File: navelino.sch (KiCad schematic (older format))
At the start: 73 parts, among them CON1 USB, IC1 ATMEGA328P-A, M1 CONN_1, M2 CONN_1, P1 CONN_02X03, P3 CONN_6, SW0 SW_PUSH, SW1 SMD-SWITCH-TACTILE-SPST-NO(4P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, SW2 SMD-SWITCH-TACTILE-SPST-NO(4P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, U1 XC6204B332MR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

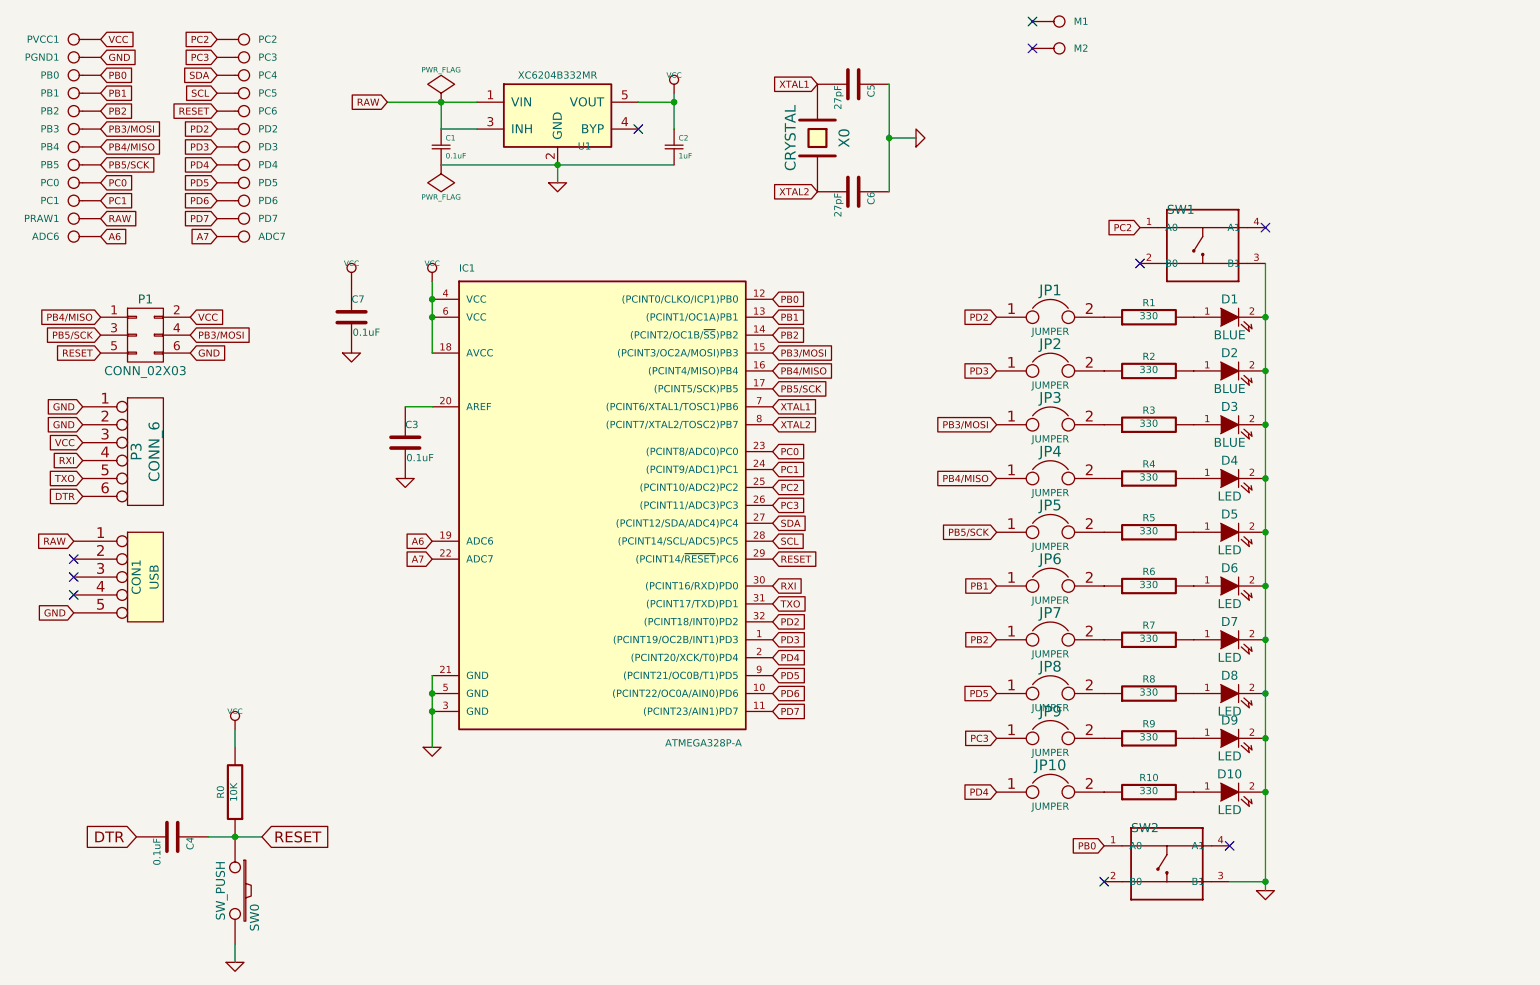
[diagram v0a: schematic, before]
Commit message: Empezando rev3
- Permitir hojas intercambiables, conector SPI completo
- Usar charlieplexing para reducir el numero de GPIOS para los leds a 4
en vez de 10
- Eliminar el botón de reset, se usara una pulsación prolongada de los
dos botones de disparo para hacer un reset software
- Añadir soporte V-USB en el cuerpo
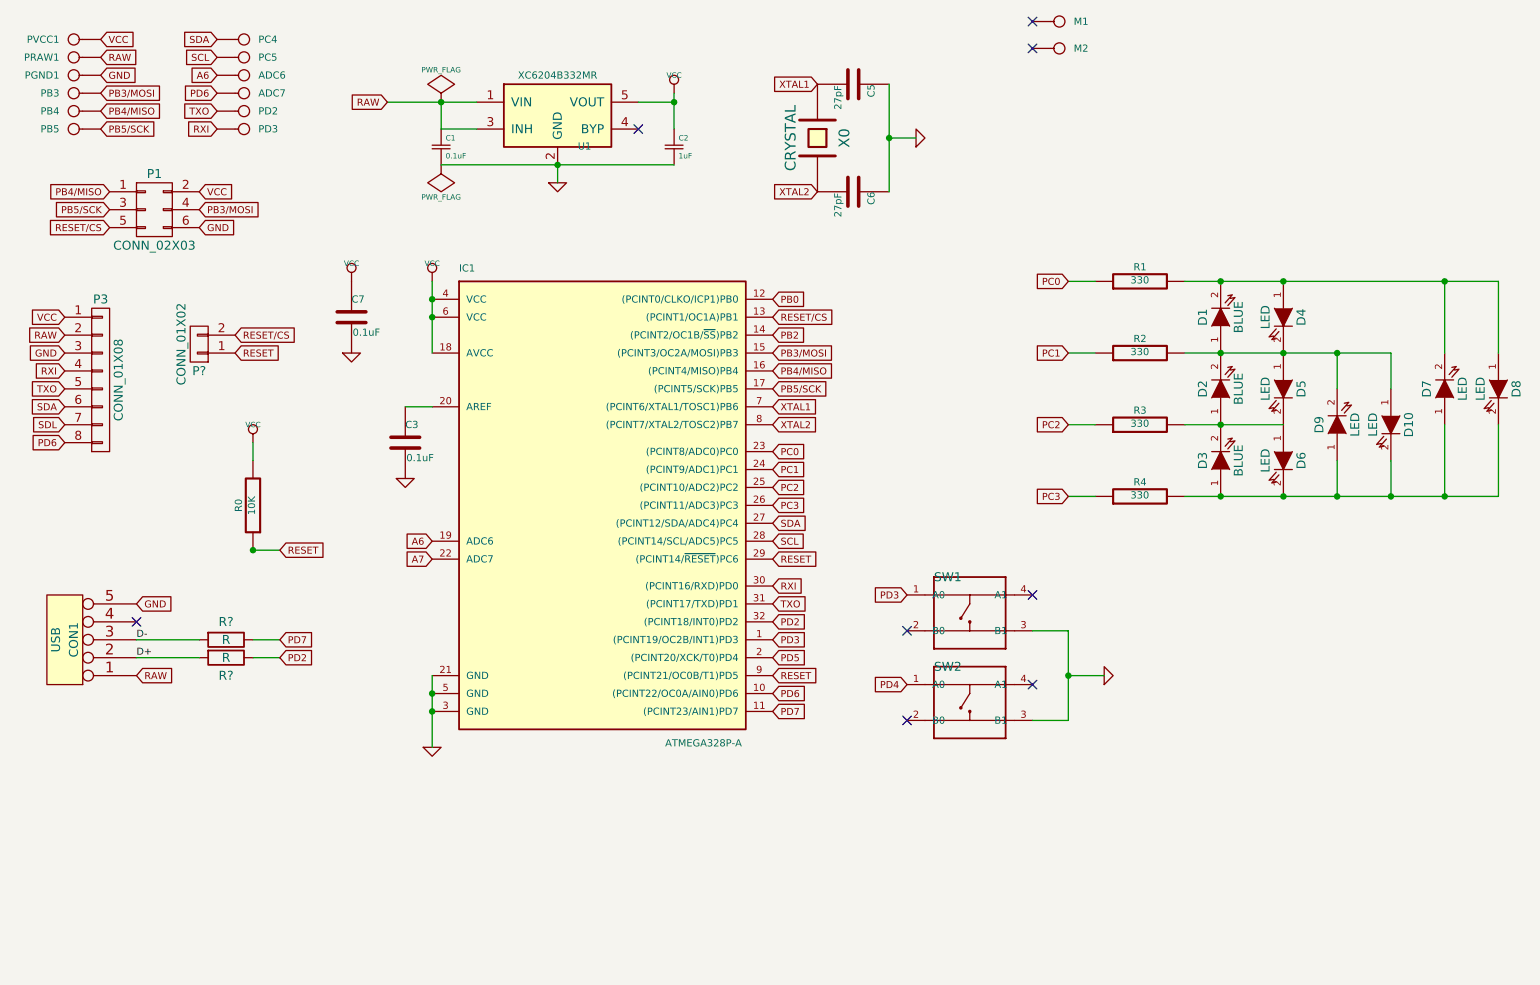
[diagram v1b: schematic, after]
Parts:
- removed C4: 0.1uF, navelino:C_0805, symbol C-RESCUE-navelino
- removed JP1, JP10, JP2, JP3, JP4, JP5, JP6, JP7, JP8, JP9: JUMPER, navelino:PCB_JUMPER, symbol JUMPER
- removed P3: CONN_6, navelino:Pin_Header_Angled_1x06, symbol CONN_6
- removed PB0, PB1, PB2, PC0, PC1, PC2, PC3, PC6, PD4, PD5, PD6, PD7: CONN_1, navelino:SolderWirePad_single_1mmDrill, symbol CONN_1
- removed R10, R5, R6, R7, R8, R9: 330, navelino:R_0805_HandSoldering, symbol R-RESCUE-navelino
- removed SW0: SW_PUSH, navelino:B3U-1000P, symbol SW_PUSH
- added P3: CONN_01X08, symbol CONN_01X08
- added P?: CONN_01X02, symbol CONN_01X02
- added R? (x2): R, symbol R
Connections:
- net A7: no longer ADC7.1
- net GND: now also P3.3 (P3); no longer D1.2 (K), D10.2 (K), D2.2 (K), D3.2 (K), D4.2 (K), D5.2 (K), D6.2 (K), D7.2 (K), D8.2 (K), D9.2 (K)
- net PB0: no longer SW2.1 (A0)
- net PC0: now also R1.1
- net PC1: now also R2.1
- net PC2: now also R3.1; no longer SW1.1 (A0)
- net PC3: now also R4.1
- net PD2: now also R?.1; no longer PD2.1
- net PD3: now also SW1.1 (A0); no longer PD3.1
- net PD4: now also SW2.1 (A0); no longer IC1.2 ((PCINT20/XCK/T0)PD4)
- net PD5: now also IC1.2 ((PCINT20/XCK/T0)PD4); no longer IC1.9 ((PCINT21/OC0B/T1)PD5)
- net PD6: now also ADC7.1, P3.8 (P8)
- net PD7: now also R?.1
- net RAW: now also P3.2 (P2)
- net RESET: now also IC1.9 ((PCINT21/OC0B/T1)PD5), P?.1 (P1); no longer P1.5 (P5)
- net RXI: now also PD3.1, P3.4 (P4)
- net SDA: now also P3.6 (P6)
- net TXO: now also PD2.1, P3.5 (P5)
- net VCC: now also P3.1 (P1)
- net at D1.1 (A): now also D10.1 (A), D2.2 (K), D4.2 (K), D5.1 (A), D9.2 (K), R2.2; no longer R1.2
- net at D2.1 (A): now also D3.2 (K), D5.2 (K), D6.1 (A), R3.2; no longer R2.2
- net at D3.1 (A): now also D10.2 (K), D6.2 (K), D7.1 (A), D8.2 (K), D9.1 (A), R4.2; no longer R3.2
- net at D4.1 (A): now also D1.2 (K), D7.2 (K), D8.1 (A), R1.2; no longer R4.2
- net D+: now reaches CON1.2
- net D+: now also R?.2
- net D-: now reaches CON1.3
- net D-: now also R?.2
- net PB1 renamed RESET/CS
- net RESET/CS: now also P1.5 (P5), P?.2 (P2)
- new net SDL: P3.7 (P7)
- no-connect marks 10 -> 8
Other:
- moved on the sheet: ADC6, ADC7, CON1, D1, D10, D2, D3, D4, D5, D6, D7, D8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

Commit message: Casi finalizado el nuevo esquema
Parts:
- removed M1, M2: CONN_1, navelino:SolderWirePad_single_1mmDrill, symbol CONN_1
- removed P1: CONN_02X03, navelino:ISPSMD, symbol CONN_02X03
- removed P?: CONN_01X02, symbol CONN_01X02
- added P1: CONN_02X04, symbol CONN_02X04
- added R5: R, symbol R
- R6, R7: renamed from R?; value R -> 68
- renumbered PB3 to PB0, PB4 to PB1, PB5 to PB2
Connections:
- net PB0 is gone; now on net RESET: IC1.12 ((PCINT0/CLKO/ICP1)PB0)
- net SDL is gone; now on net SCL: P3.7 (P7)
- net A6: now also PD3.1; no longer ADC6.1
- net A7: now also PB2.1
- net D-: now also R5.2
- net GND: now also P1.6 (P6)
- net PB3/MOSI: now also P1.4 (P4); no longer PB0.1
- net PB4/MISO: now also P1.1 (P1); no longer PB1.1
- net PB5/SCK: now also P1.3 (P3); no longer PB2.1
- net PD4: now also IC1.2 ((PCINT20/XCK/T0)PD4)
- net PD5: now also IC1.9 ((PCINT21/OC0B/T1)PD5), PB1.1; no longer IC1.2 ((PCINT20/XCK/T0)PD4)
- net PD6: now also PD2.1; no longer ADC7.1
- net RESET: now also P1.5 (P5); no longer IC1.9 ((PCINT21/OC0B/T1)PD5)
- net RXI: now also ADC7.1, P1.7 (P7); no longer PD3.1
- net TXO: now also ADC6.1, P1.8 (P8); no longer PD2.1
- net VCC: now also P1.2 (P2), R5.1
- net PB2: no longer names the net of IC1.14 ((PCINT2/OC1B/~SS~)PB2)
- net RESET/CS renamed PB1
- net PB1: now also PB0.1
- no-connect marks 8 -> 7
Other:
- moved on the sheet: C7, CON1, D1, D10, D2, D3, D4, D5, D6, D7, D8, D9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
